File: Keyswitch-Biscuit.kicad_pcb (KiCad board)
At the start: 2 copper layers, 17.8 x 17.8 mm, 11 parts, among them J1 Conn_01x03_Male, J2 Conn_01x03_Male, J3 Conn_01x03_Male, J4 Conn_01x03_Male

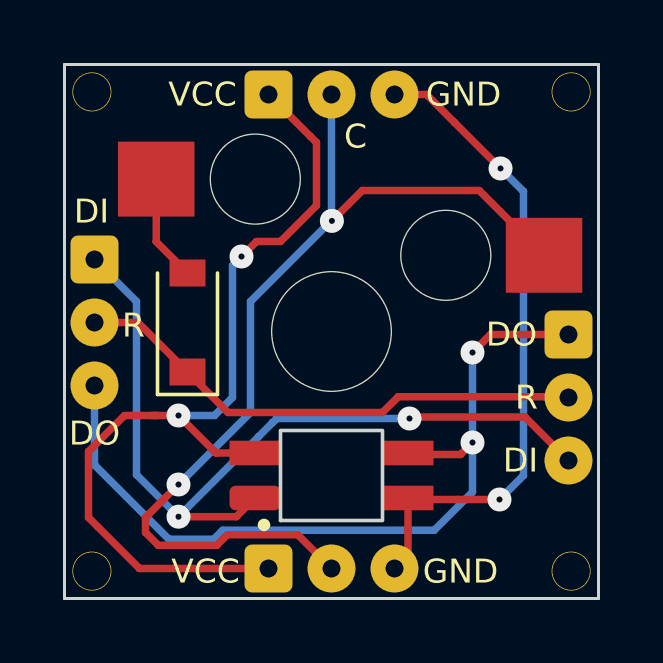
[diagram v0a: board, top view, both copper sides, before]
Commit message: Updated RGB LED footprint to match reversed variant. Retraced All. Replaced corner holes for notches.
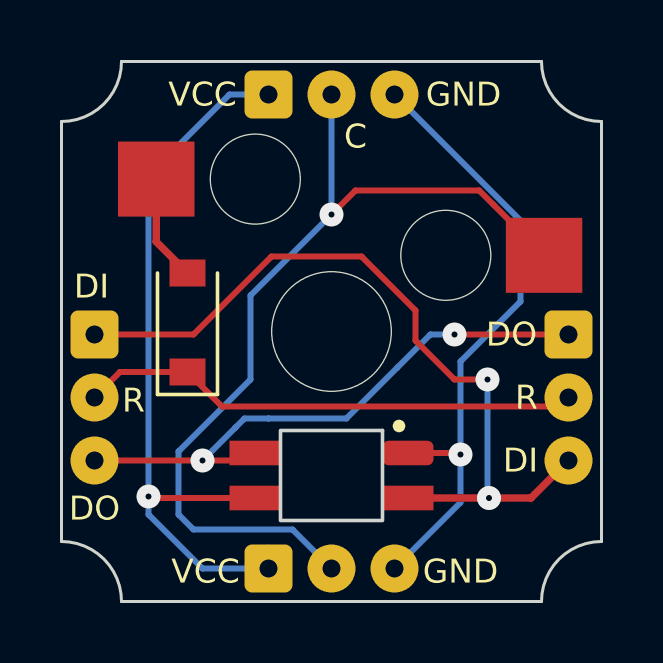
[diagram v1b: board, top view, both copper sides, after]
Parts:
- removed REF** (x4): MountingHole_2.1mm, MountingHole:MountingHole_2.1mm
- moved J4 2.50 mm to (101.0, 109.0)
- turned D2 to 0 degrees
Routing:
- net DataOut: track 27.5 -> 19.7 mm
- net VCC: track 30.1 -> 25.4 mm, vias 2 -> 1
- net Col: track 32.6 -> 30.3 mm, vias 2 -> 1
- net DataIn: track 28.2 -> 26.9 mm
- net GND: track 21.8 -> 21.2 mm, vias 2 -> 1
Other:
- board size 17.8 x 17.8 mm -> 18 x 18 mm
- board text added: "V1.1"
- board text removed: "V1.0"
